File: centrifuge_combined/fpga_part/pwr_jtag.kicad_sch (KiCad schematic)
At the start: 67 parts, among them J1 Conn_02x07_Odd_Even, SW1 SW_MEC_5E, U1 XC7A100T-FTG256, U15 D5V0FS4U10LP

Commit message: Almost finished releasable version
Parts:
- added TP1: TestPoint, TestPoint:TestPoint_Keystone_5015_Micro-Minature, symbol Connector:TestPoint
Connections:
- net INIT_B: now also TP1.1
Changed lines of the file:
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@@
   (junction (at 223.52 121.92) (diameter 0) (color 0 0 0 0)
+  )
+  (junction (at 166.4208 81.28) (diameter 0) (color 0 0 0 0)
   )
   (junction (at 152.4 103.505) (diameter 0) (color 0 0 0 0)
@@
     (stroke (width 0) (type default) (color 0 0 0 0))
   )
-  (wire (pts (xy 102.87 81.28) (xy 189.865 81.28))
+  (wire (pts (xy 102.87 81.28) (xy 166.4208 81.28))
     (stroke (width 0) (type default) (color 0 0 0 0))
   )
@@
     (stroke (width 0) (type default) (color 0 0 0 0))
   )
+  (wire (pts (xy 166.4208 81.28) (xy 189.865 81.28))
+    (stroke (width 0) (type default) (color 0 0 0 0))
+  )
   (wire (pts (xy 223.52 134.62) (xy 223.52 137.16))
     (stroke (width 0) (type default) (color 0 0 0 0))
@@
   )
   (wire (pts (xy 180.34 78.74) (xy 181.61 78.74))
+    (stroke (width 0) (type default) (color 0 0 0 0))
+  )
+  (wire (pts (xy 166.4208 75.2348) (xy 166.4208 81.28))
     (stroke (width 0) (type default) (color 0 0 0 0))
   )
@@
     (pin "2")
   )
+  (symbol (lib_id "Connector:TestPoint") (at 166.4208 75.2348 0) (unit 1)
+    (in_bom yes) (on_board yes) (fields_autoplaced)
+    (property "Reference" "TP1" (id 0) (at 168.3258 70.6627 0)
+      (effects (font (size 1.27 1.27)) (justify left))
+    )
+    (property "Value" "TestPoint" (id 1) (at 168.3258 73.2027 0)
+      (effects (font (size 1.27 1.27)) (justify left))
+    )
+    (property "Footprint" "TestPoint:TestPoint_Keystone_5015_Micro-Minature" (id 2) (at 171.5008 75.2348 0)
+      (effects (font (size 1.27 1.27)) hide)
+    )
+    (property "Datasheet" "~" (id 3) (at 171.5008 75.2348 0)
+      (effects (font (size 1.27 1.27)) hide)
+    )
+    (property "Order Page" "https://no.mouser.com/ProductDetail/Keystone-Electronics/5015?qs=qOqV1E1P08ShW56PtUq2FA%3D%3D" (id 4) (at 166.4208 75.2348 0)
+      (effects (font (size 1.27 1.27)) hide)
+    )
+    (pin "1")
+  )
   (symbol (lib_id "Device:C_Small") (at 99.695 182.88 0) (unit 1)

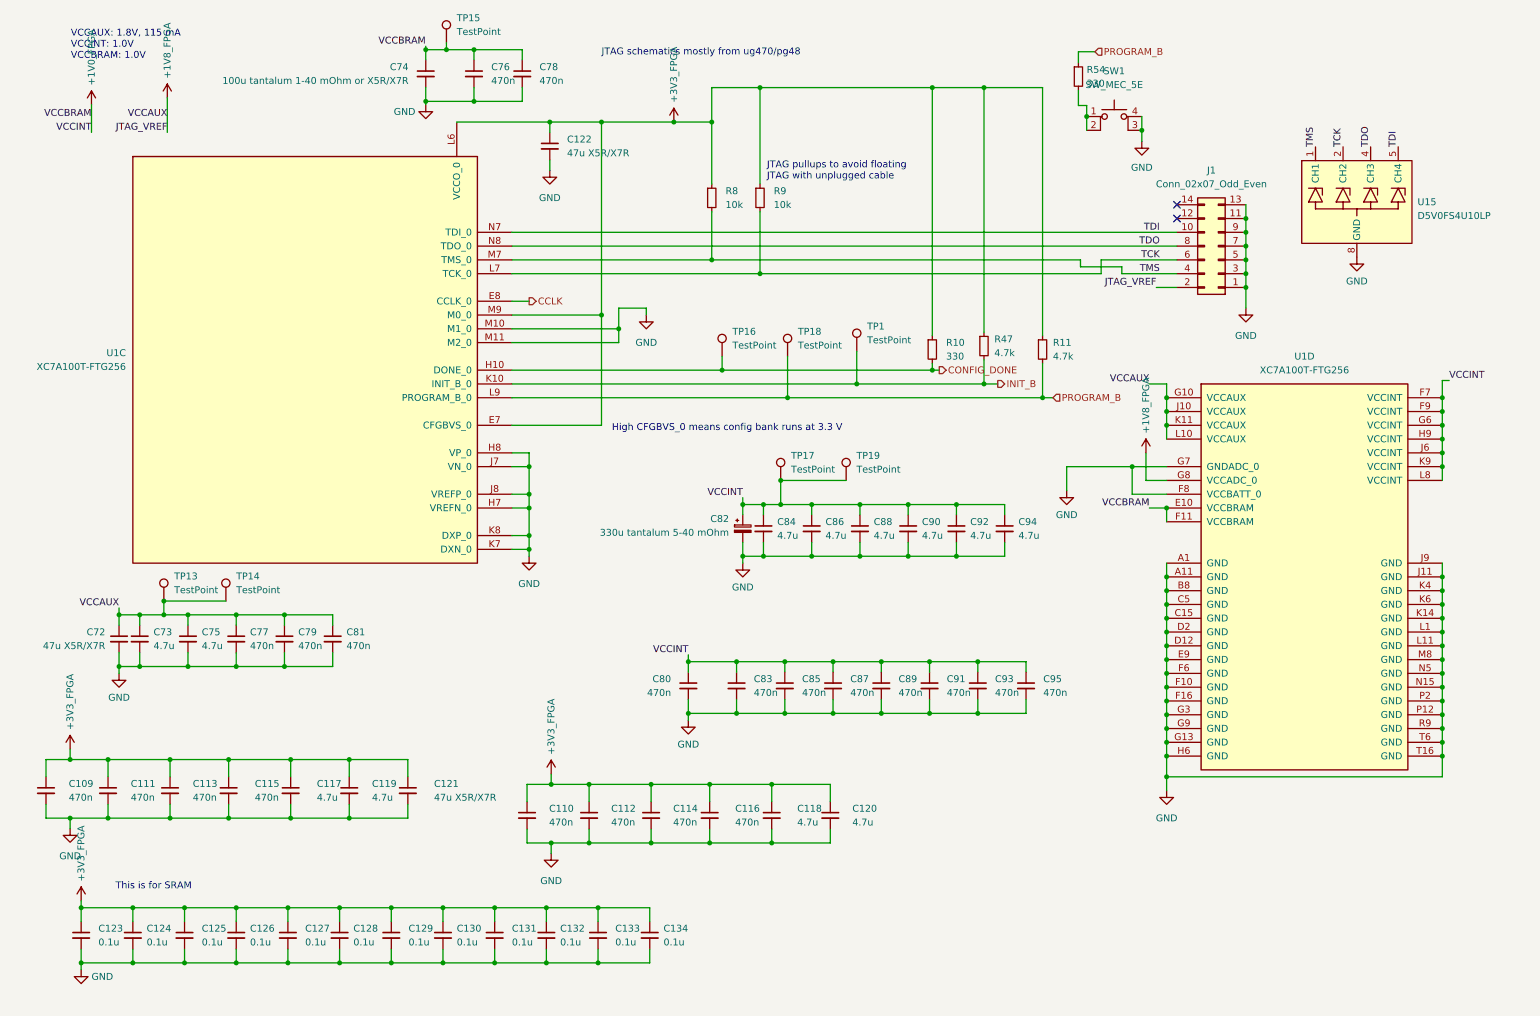
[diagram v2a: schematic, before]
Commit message: Fixed missing footprints, added decoupling capacitors, adjusted board edges
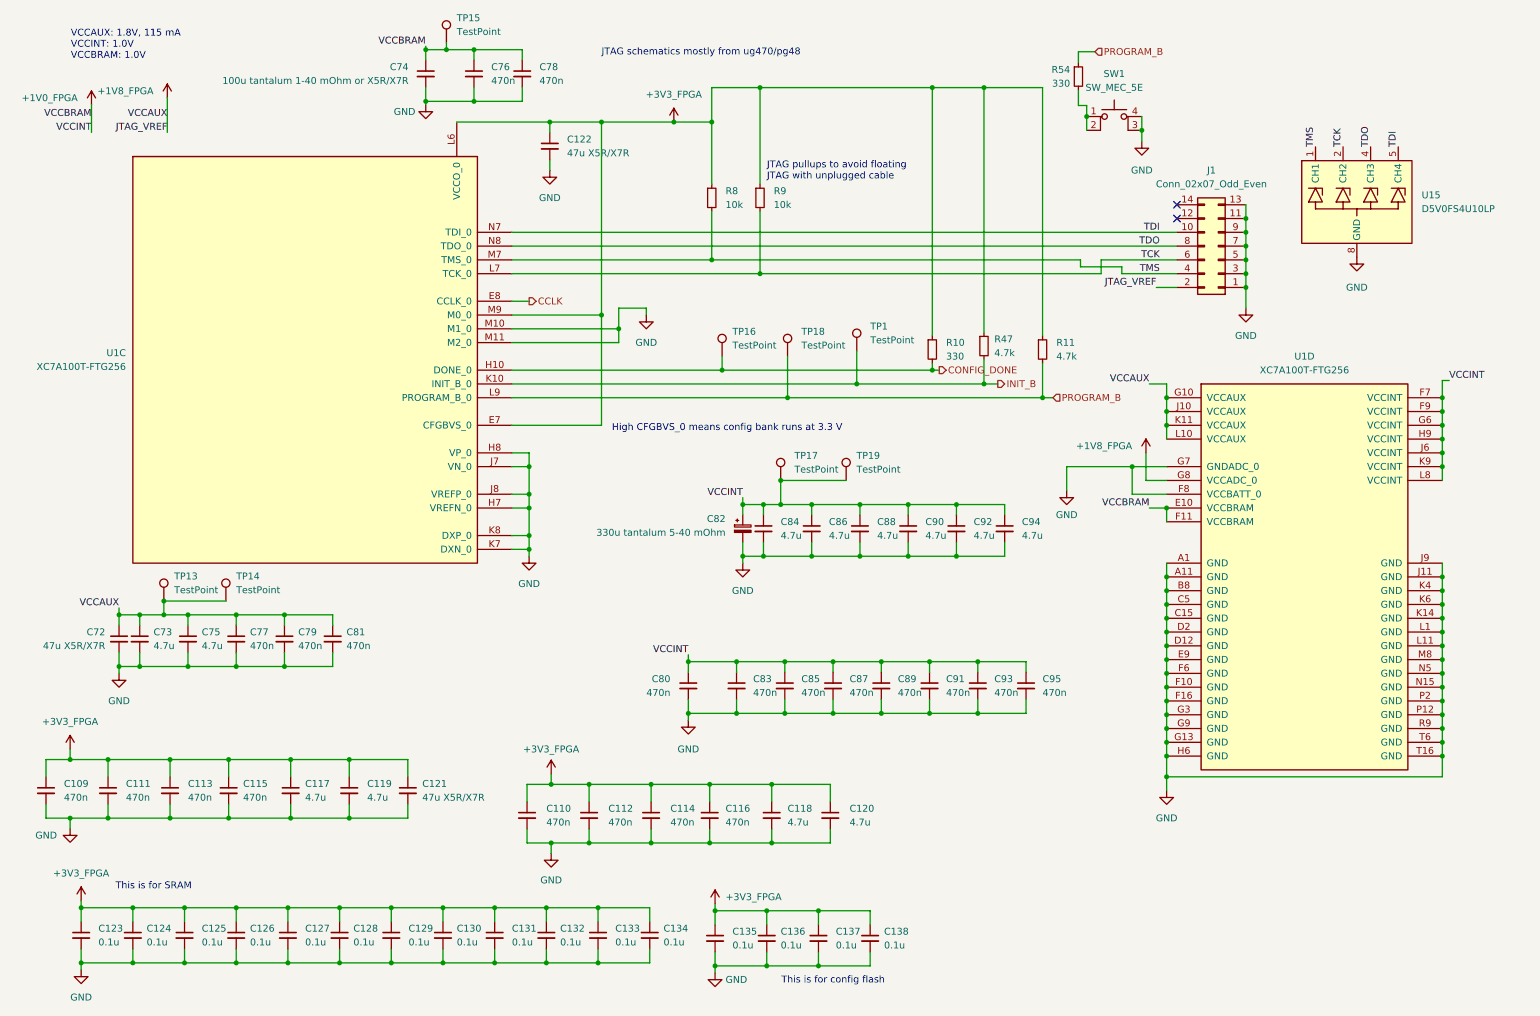
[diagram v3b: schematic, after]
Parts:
- added C135, C136, C137, C138: 0.1u, Capacitor_SMD:C_0805_2012Metric_Pad1.18x1.45mm_HandSolder, symbol Device:C_Small
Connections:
- net +3V3_FPGA: now also C135.1, C136.1, C137.1, C138.1
- net GND: now also C135.2, C136.2, C137.2, C138.2
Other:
- note added: "This is for config flash"

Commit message: remove digikey links to products that we already buy from mouser, add mouser link instead
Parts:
- J1: Order Page https://www.digikey.no/en/products/detail/molex/0878311411/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 -> BOUGHT https://www.digikey.no/en/products/detail/molex/0878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
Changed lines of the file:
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@@
       (effects (font (size 1.27 1.27)) hide)
     )
-    (property "Order Page" "https://www.digikey.no/en/products/detail/molex/0878311411/3313107" (id 4) (at 233.045 55.88 0)
+    (property "Order Page" "BOUGHT https://www.digikey.no/en/products/detail/molex/0878311411/3313107" (id 4) (at 233.045 55.88 0)
       (effects (font (size 1.27 1.27)) hide)
     )

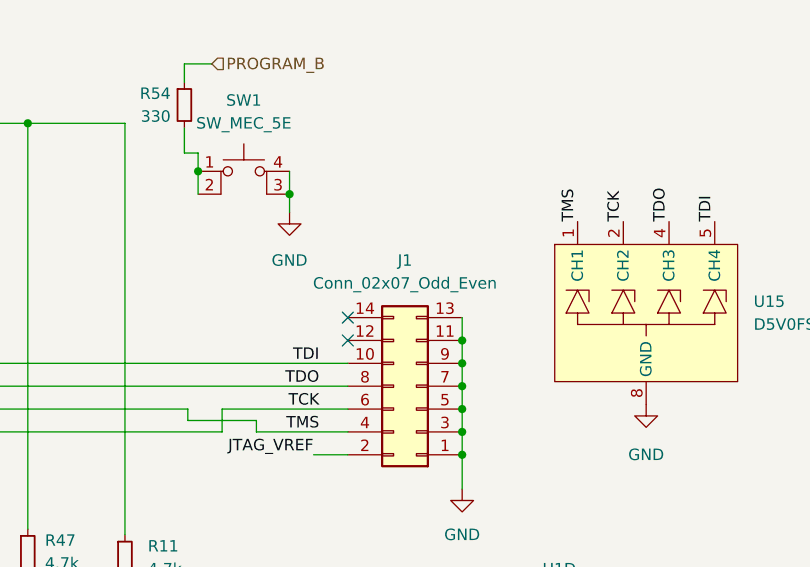
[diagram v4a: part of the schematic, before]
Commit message: more checks, also make silkscreen text for connectors
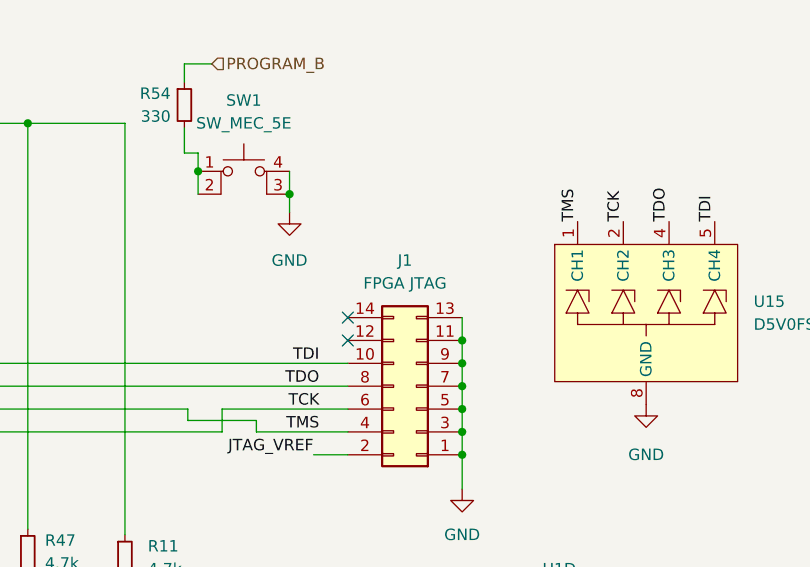
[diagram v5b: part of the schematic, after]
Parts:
- J1: value Conn_02x07_Odd_Even -> FPGA JTAG
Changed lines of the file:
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@@
     (in_bom yes) (on_board yes) (fields_autoplaced)
     (property "Reference" "J1" (id 0) (at 231.775 41.91 0))
-    (property "Value" "Conn_02x07_Odd_Even" (id 1) (at 231.775 44.45 0))
+    (property "Value" "FPGA JTAG" (id 1) (at 231.775 44.45 0))
     (property "Footprint" "centrifuge footprints:878311411" (id 2) (at 233.045 55.88 0)
       (effects (font (size 1.27 1.27)) hide)

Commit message: fix JTAG Vref, pullup on CS and remove SRAM_CS1p3
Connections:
- net +1V8_FPGA: no longer J1.2 (Pin_2)
- net +3V3_FPGA: now also J1.2 (Pin_2)
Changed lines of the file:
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@@
     (stroke (width 0) (type default) (color 0 0 0 0))
   )
-  (wire (pts (xy 25.4 29.845) (xy 25.4 34.925))
+  (wire (pts (xy 25.4 29.845) (xy 25.4 36.83))
     (stroke (width 0) (type default) (color 0 0 0 0))
   )
@@
     (stroke (width 0) (type default) (color 0 0 0 0))
   )
-  (wire (pts (xy 39.37 28.575) (xy 39.37 34.925))
+  (wire (pts (xy 39.37 28.575) (xy 39.37 36.195))
     (stroke (width 0) (type default) (color 0 0 0 0))
   )
@@
     (effects (font (size 1.27 1.27)) (justify right bottom))
   )
-  (label "VCCAUX" (at 39.37 32.385 180)
+  (label "VCCAUX" (at 39.37 36.195 180)
     (effects (font (size 1.27 1.27)) (justify right bottom))
   )
@@
     (effects (font (size 1.27 1.27)) (justify right bottom))
   )
-  (label "VCCBRAM" (at 25.4 32.385 180)
+  (label "VCCBRAM" (at 25.4 34.925 180)
     (effects (font (size 1.27 1.27)) (justify right bottom))
   )
@@
     (effects (font (size 1.27 1.27)) (justify left bottom))
   )
-  (label "JTAG_VREF" (at 221.615 63.5 180)
-    (effects (font (size 1.27 1.27)) (justify right bottom))
-  )
   (label "VCCINT" (at 145.415 102.235 180)
     (effects (font (size 1.27 1.27)) (justify right bottom))
@@
     (effects (font (size 1.27 1.27)) (justify right bottom))
   )
-  (label "JTAG_VREF" (at 39.37 34.925 180)
-    (effects (font (size 1.27 1.27)) (justify right bottom))
-  )
   (label "VCCINT" (at 135.382 131.191 180)
     (effects (font (size 1.27 1.27)) (justify right bottom))
@@
     (effects (font (size 1.27 1.27)) (justify left bottom))
   )
-  (label "VCCINT" (at 25.4 34.925 180)
+  (label "VCCINT" (at 25.4 36.83 180)
     (effects (font (size 1.27 1.27)) (justify right bottom))
   )
@@
   )
   (symbol (lib_id "Device:C_Small") (at 197.612 136.906 0) (unit 1)
-    (in_bom yes) (on_board yes) (fields_autoplaced)
+    (in_bom yes) (on_board yes)
     (property "Reference" "C95" (id 0) (at 200.66 135.6422 0)
       (effects (font (size 1.27 1.27)) (justify left))
@@
     (pin "2")
   )
+  (symbol (lib_id "centrifuge_symbols:+3V3_FPGA") (at 221.615 63.5 180) (unit 1)
+    (in_bom yes) (on_board yes) (fields_autoplaced)
+    (property "Reference" "#PWR03" (id 0) (at 221.615 59.69 0)
+      (effects (font (size 1.27 1.27)) hide)
+    )
+    (property "Value" "+3V3_FPGA" (id 1) (at 221.615 68.58 0))
+    (property "Footprint" "" (id 2) (at 221.615 63.5 0)
+      (effects (font (size 1.27 1.27)) hide)
+    )
+    (property "Datasheet" "" (id 3) (at 221.615 63.5 0)
+      (effects (font (size 1.27 1.27)) hide)
+    )
+    (pin "1")
+  )
   (symbol (lib_id "Device:R_Small") (at 189.865 74.295 0) (unit 1)

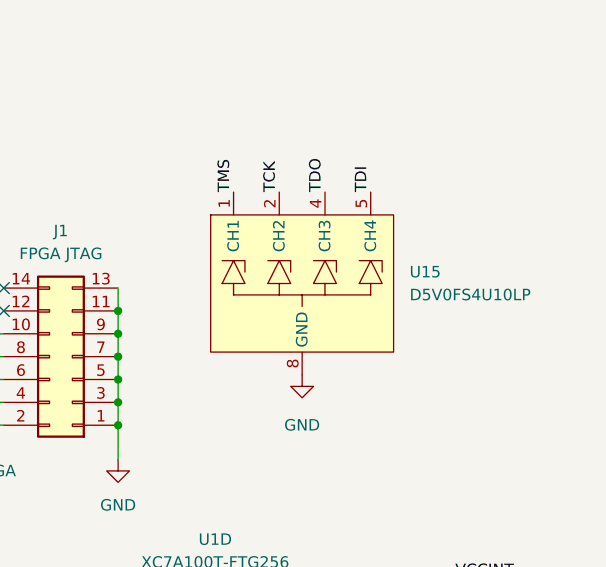
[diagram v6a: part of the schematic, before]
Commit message: make final shopping list, added to Mouser and DigiKey lists. Also budget. Swaps out TVS diodes
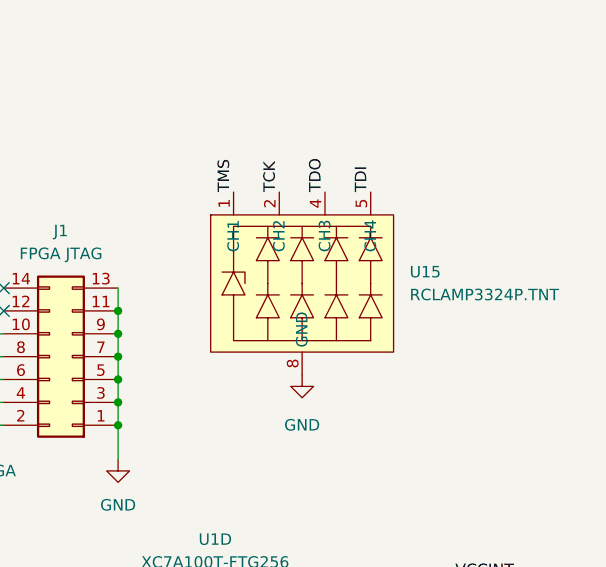
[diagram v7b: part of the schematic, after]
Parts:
- U15: value D5V0FS4U10LP -> RCLAMP3324P.TNT; symbol centrifuge_symbols:D5V0FS4U10LP -> centrifuge_symbols:RCLAMP3324P.TNT; Order Page https://www.digikey.no/en/products/detail/diodes-incorporat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 -> https://no.mouser.com/ProductDetail/Semtech/RCLAMP3324P.TNT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
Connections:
- net GND: no longer U15.3 (GND)
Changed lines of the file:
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@@
     (pin "2")
   )
-  (symbol (lib_id "centrifuge_symbols:D5V0FS4U10LP") (at 258.572 47.752 0) (unit 1)
+  (symbol (lib_id "centrifuge_symbols:RCLAMP3324P.TNT") (at 258.572 47.752 0) (unit 1)
     (in_bom yes) (on_board yes) (fields_autoplaced)
     (property "Reference" "U15" (id 0) (at 270.51 46.4819 0)
       (effects (font (size 1.27 1.27)) (justify left))
     )
-    (property "Value" "D5V0FS4U10LP" (id 1) (at 270.51 49.0219 0)
+    (property "Value" "RCLAMP3324P.TNT" (id 1) (at 270.51 49.0219 0)
       (effects (font (size 1.27 1.27)) (justify left))
     )
@@
       (effects (font (size 1.27 1.27)) hide)
     )
-    (property "Datasheet" "https://www.diodes.com/assets/Datasheets/D5V0FS4U10LP.pdf" (id 3) (at 258.572 47.752 0)
+    (property "Datasheet" "https://no.mouser.com/datasheet/2/761/SEMT_S_A0002540573_1-2575715.pdf" (id 3) (at 258.572 47.752 0)
       (effects (font (size 1.27 1.27)) hide)
     )
-    (property "Order Page" "https://www.digikey.no/en/products/detail/diodes-incorporated/D5V0FS4U10LP-7/7930773" (id 4) (at 258.572 47.752 0)
+    (property "Order Page" "https://no.mouser.com/ProductDetail/Semtech/RCLAMP3324P.TNT?qs=rBWM4%252BvDhIcjIdOyxs8eng%3D%3D" (id 4) (at 258.572 47.752 0)
       (effects (font (size 1.27 1.27)) hide)
     )

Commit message: fix duplicate Cs, add extra ACD/DAC and breakout, and fix TVS schematic hidden pin
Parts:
- U15: Order Page https://no.mouser.com/ProductDetail/Semtech/RCLAMP3324P.TNT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 -> https://www.digikey.no/en/products/detail/diodes-incorporat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
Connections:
- net GND: now also U15.3 (GND)
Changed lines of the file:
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@@
       (effects (font (size 1.27 1.27)) hide)
     )
-    (property "Datasheet" "https://no.mouser.com/datasheet/2/761/SEMT_S_A0002540573_1-2575715.pdf" (id 3) (at 258.572 47.752 0)
+    (property "Datasheet" "https://www.diodes.com/assets/Datasheets/D5V0FS4U10LP.pdf" (id 3) (at 258.572 47.752 0)
       (effects (font (size 1.27 1.27)) hide)
     )
-    (property "Order Page" "https://no.mouser.com/ProductDetail/Semtech/RCLAMP3324P.TNT?qs=rBWM4%252BvDhIcjIdOyxs8eng%3D%3D" (id 4) (at 258.572 47.752 0)
+    (property "Order Page" "https://www.digikey.no/en/products/detail/diodes-incorporated/D5V0FS4U10LP-7/7930773" (id 4) (at 258.572 47.752 0)
       (effects (font (size 1.27 1.27)) hide)
     )
